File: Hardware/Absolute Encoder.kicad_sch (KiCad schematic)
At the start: 19 parts, among them J1 PISO_OUT, J2 PISO_IN, U1 74LS165

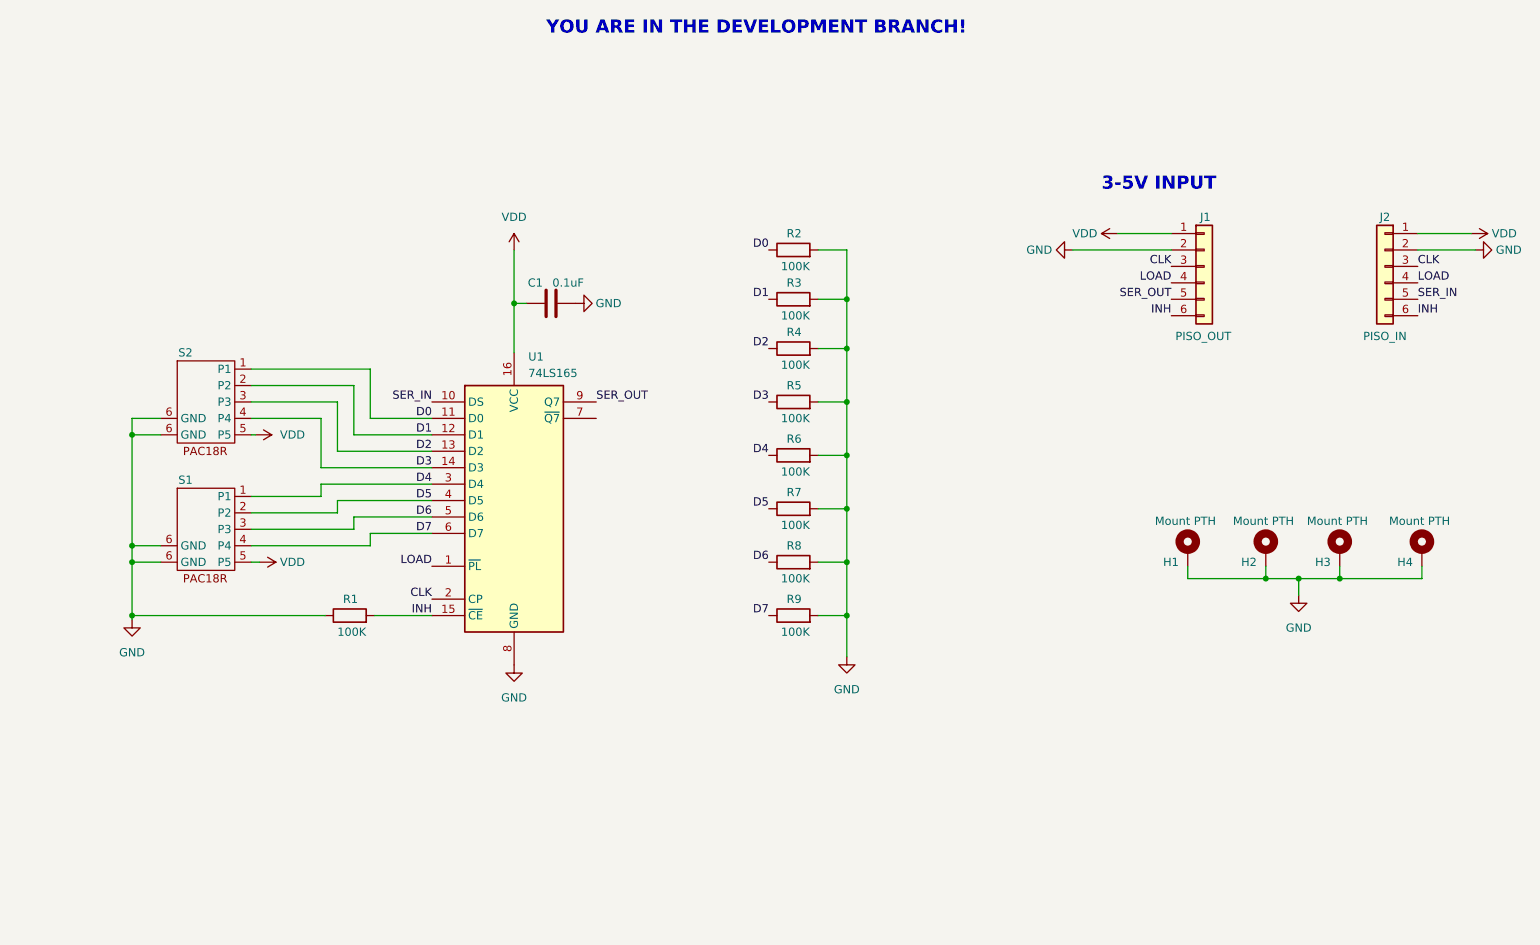
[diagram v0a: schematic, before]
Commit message: Added breakaway and set encoder distance
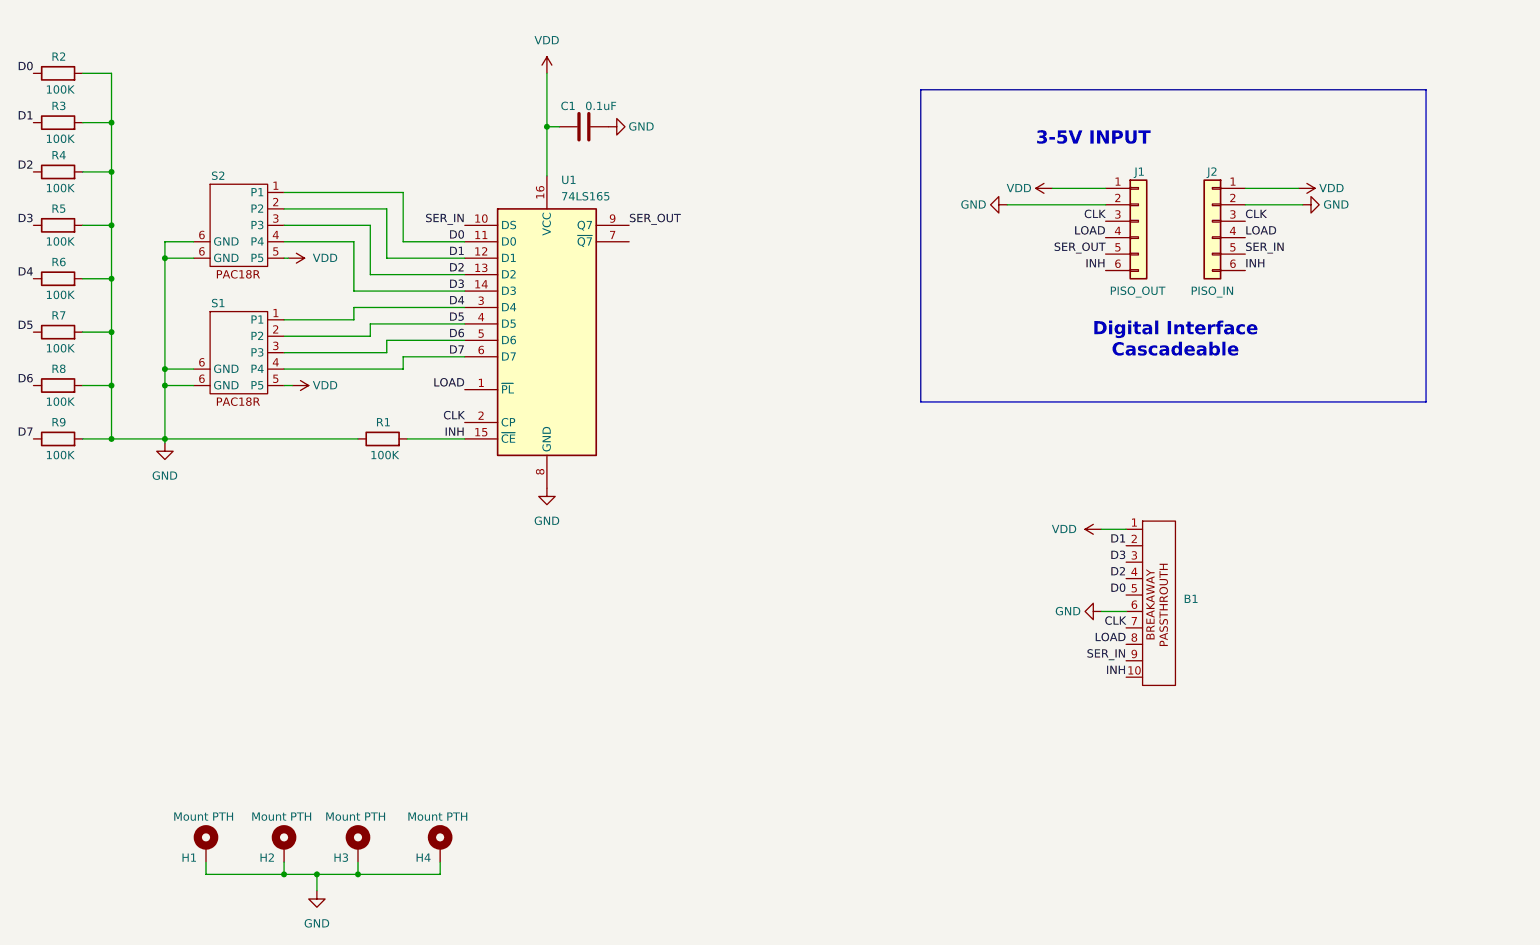
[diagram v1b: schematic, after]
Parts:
- added B1: ~, AbsoluteEncoder:Breakaway_10pos, symbol AbsoluteEncoder_Library:Breakaway_10pos
- R1, R2, R3, R4, R5, R6, R7, R8, R9: footprint Resistor_SMD:R_0402_1005Metric -> Resistor_SMD:R_0603_1608Metric
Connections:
- net CLK: now also B1.7
- net D0: now also B1.5
- net D1: now also B1.2
- net D2: now also B1.4
- net D3: now also B1.3
- net GND: now also B1.6
- net INH: now also B1.10
- net LOAD: now also B1.8
- net SER_IN: now also B1.9
- net VDD: now also B1.1
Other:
- note added: "Digital Interface Cascadeable"
- note removed: "YOU ARE IN THE DEVELOPMENT BRANCH!"
- moved on the sheet: C1, H1, H2, H3, H4, J1, J2, R1, R2, R3, R4, R5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
